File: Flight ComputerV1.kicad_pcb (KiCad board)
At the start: 4 copper layers, 100 x 100 mm, 37 parts, among them J101 ICSP, J102 Screw_Terminal_01x02, J103 Conn_01x08, J104 Conn_01x07, J105 Micro_SD_Card, J106 Conn_02x10_Top_Bottom, J201 Conn_Coaxial, SW101 1-1825910-8, U101 ATmega328PB-A, U102 LMT84DCK, U201 RXM-GPS-RM-T, U301 LIS3MDLTR, U302 LSM6DSOXTR

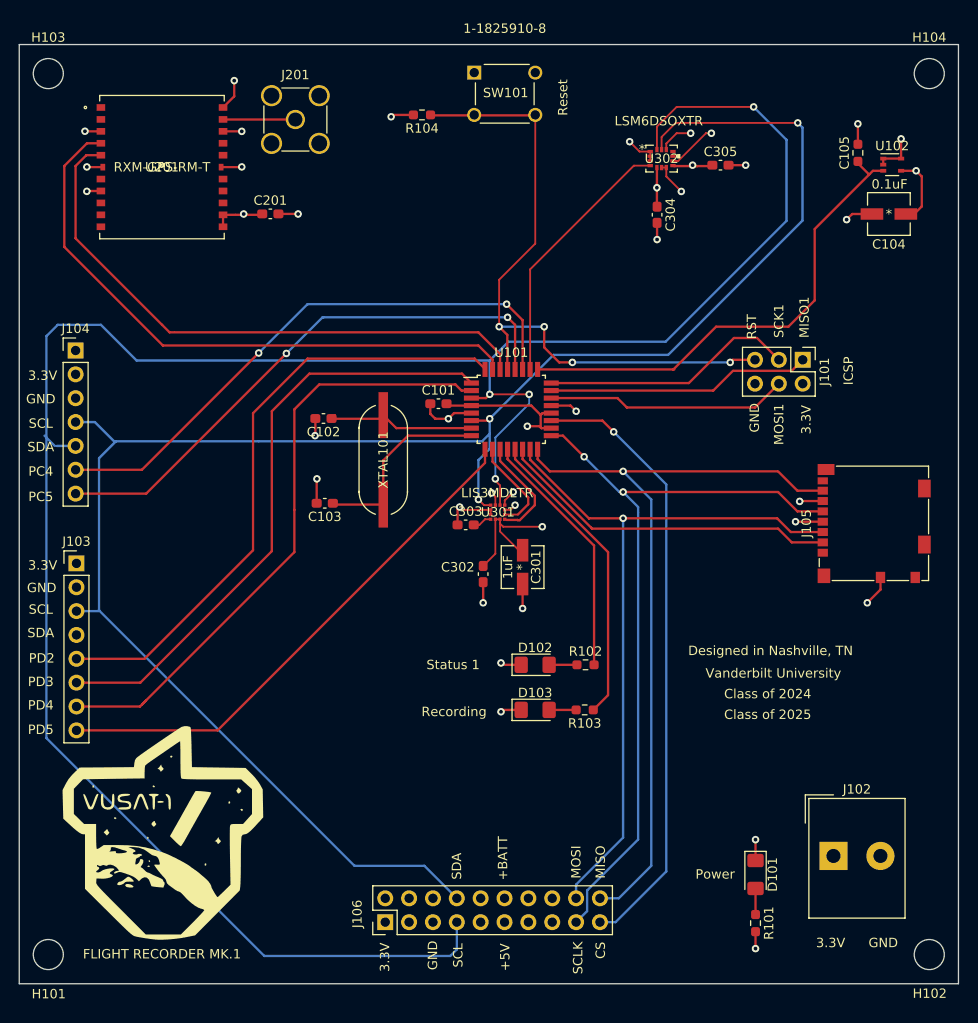
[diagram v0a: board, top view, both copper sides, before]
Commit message: Adjusted copper trace widths
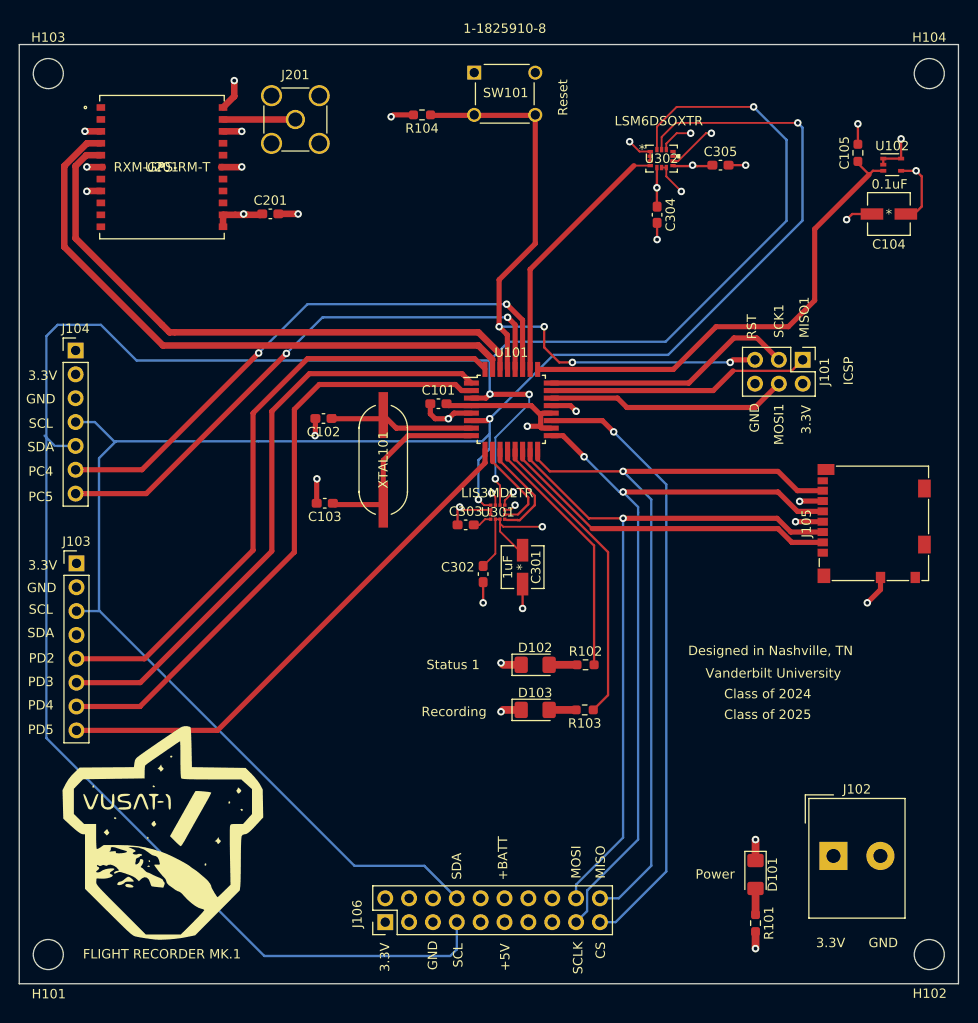
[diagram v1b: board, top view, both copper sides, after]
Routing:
- net /PD4: track 66.0 -> 65.4 mm

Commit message: Adjusted one minor back copper trace
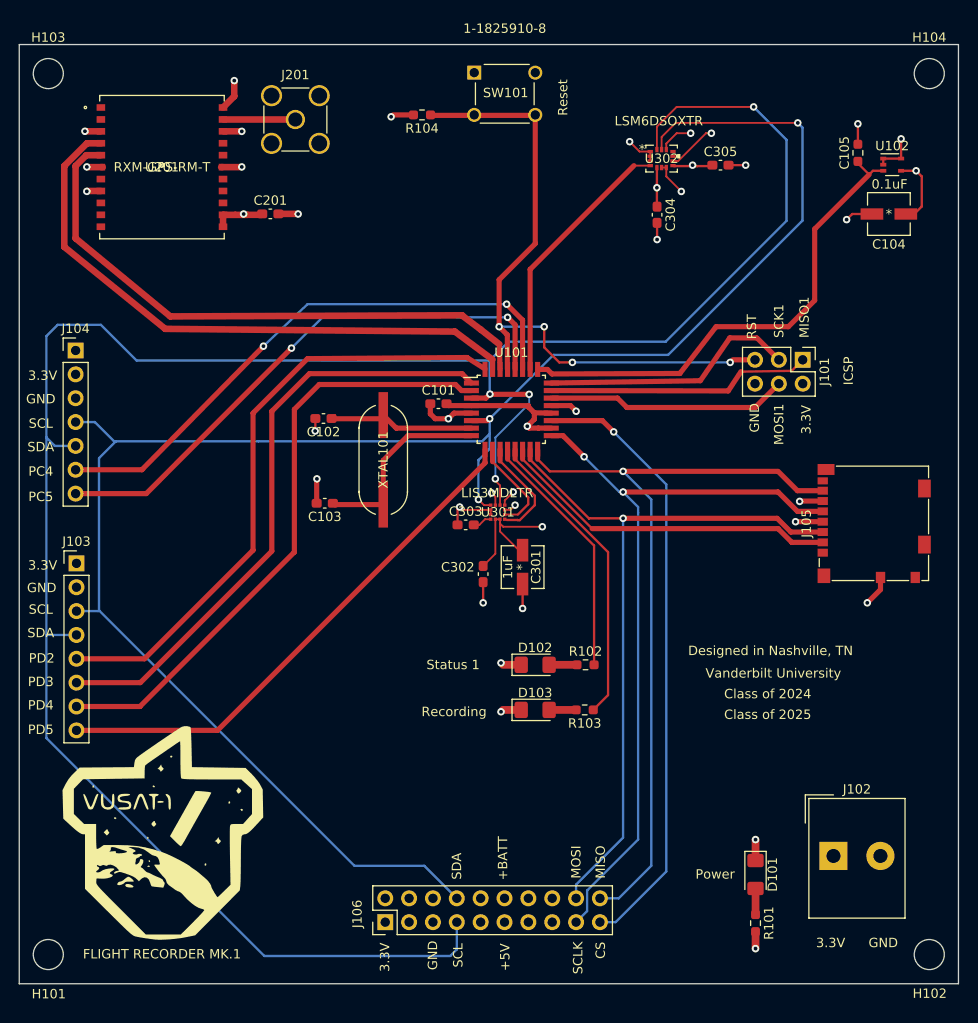
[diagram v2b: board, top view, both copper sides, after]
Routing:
- net SDA: track 240.5 -> 243.6 mm
- net TX: track 65.1 -> 64.2 mm
- net /T_OUT1: track 52.0 -> 52.7 mm
- net /PC5: track 59.7 -> 60.4 mm
- net GND: track 79.8 -> 79.3 mm
